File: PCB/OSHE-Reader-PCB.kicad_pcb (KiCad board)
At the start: 2 copper layers, 46 parts, among them Q1 Si1308EDL, Q2 BSS138, Q3 BSS138

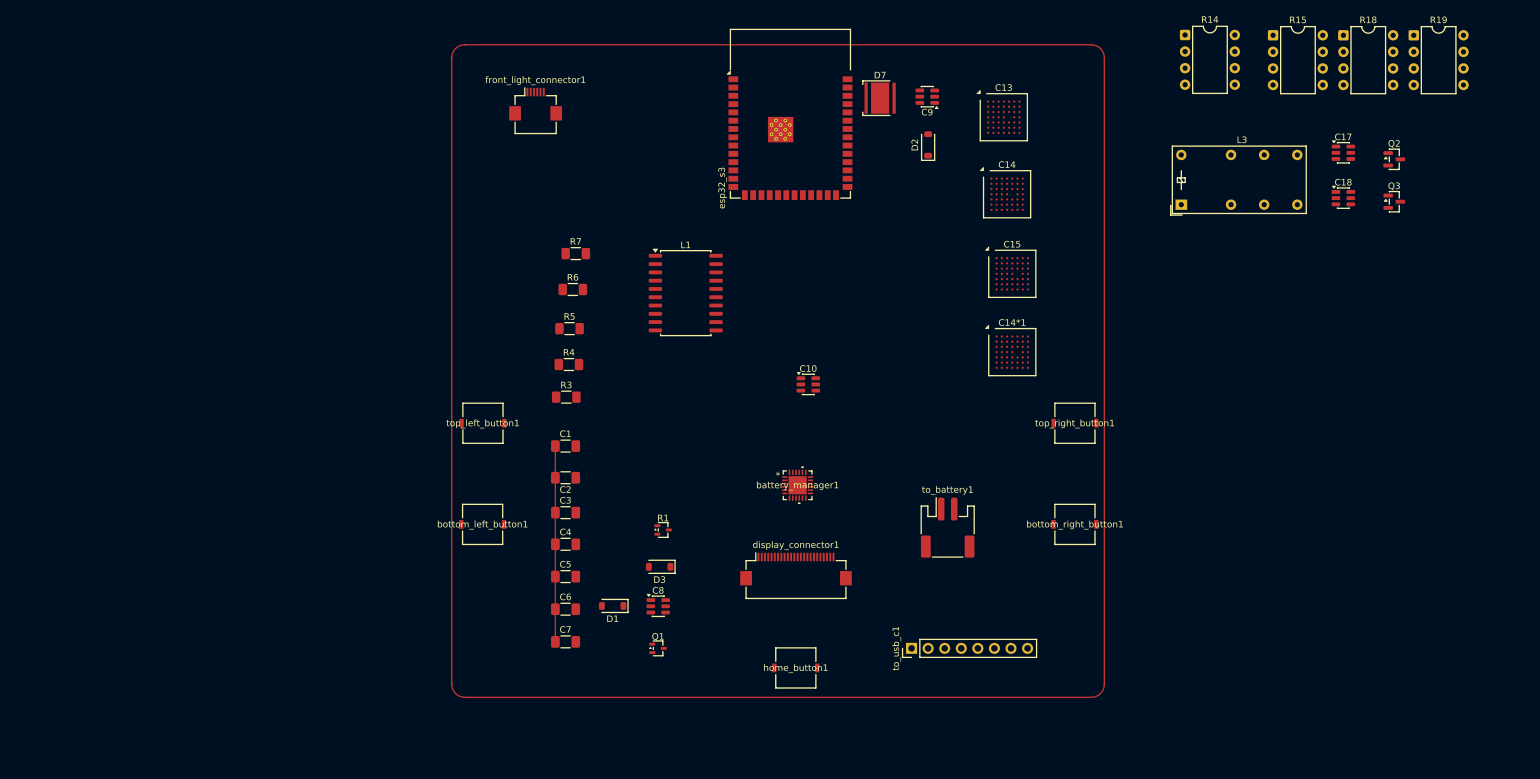
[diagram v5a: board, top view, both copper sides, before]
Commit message: PCB and BOM
Pulled stuff onto the PCB and regenerated the BOM to go into ours. Found some components (mostly caps and resistors) that are missing values so will need to update those.
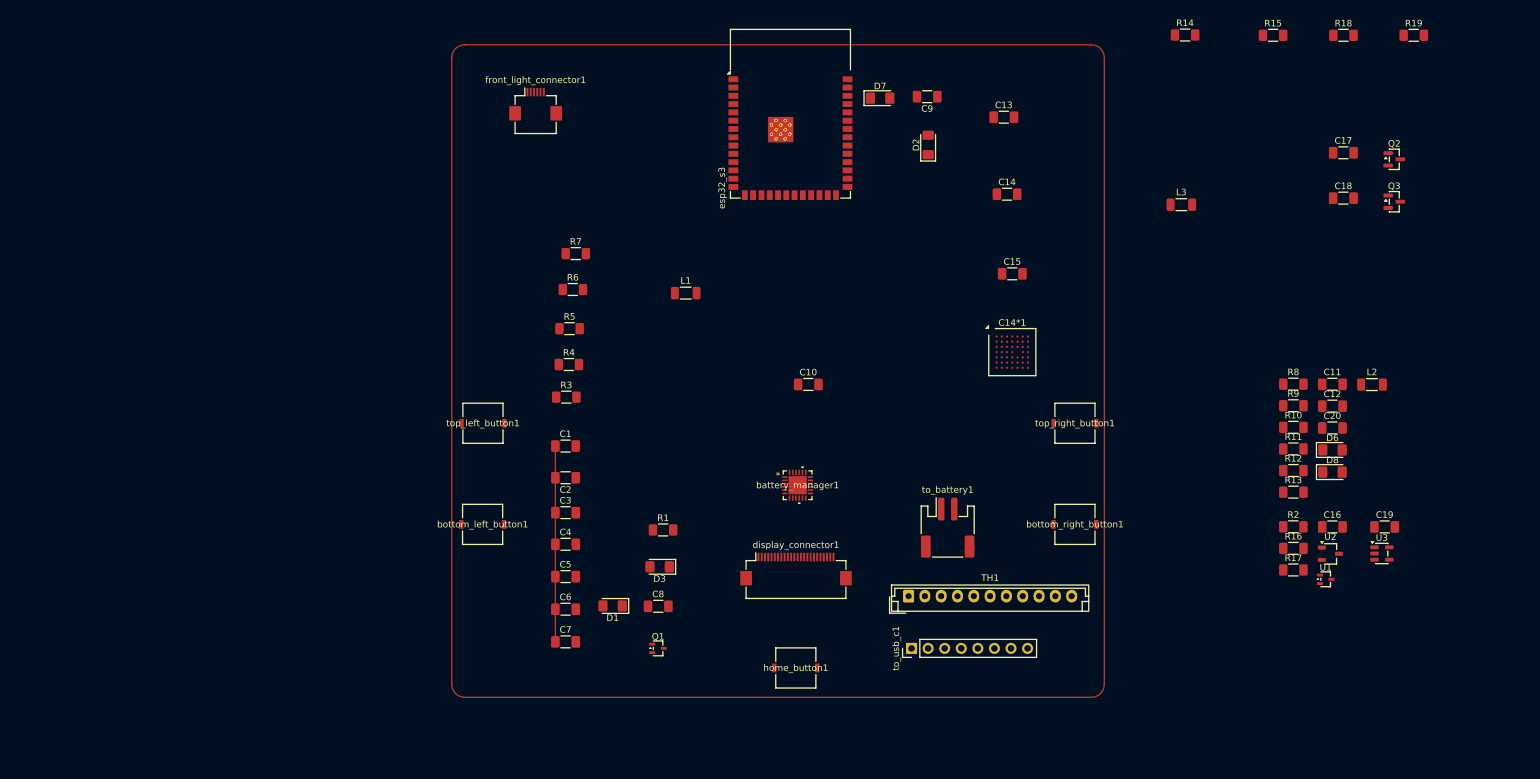
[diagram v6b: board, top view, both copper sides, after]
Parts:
- added C11: 1uF, Capacitor_SMD:C_1206_3216Metric_Pad1.33x1.80mm_HandSolder, F.Cu at (227.0, 90.0)
- added C12: 10uF, Capacitor_SMD:C_1206_3216Metric_Pad1.33x1.80mm_HandSolder, F.Cu at (227.0, 93.4)
- added C16: 0.1u, Capacitor_SMD:C_1206_3216Metric_Pad1.33x1.80mm_HandSolder, F.Cu at (227.0, 111.9)
- added C19: 10uF, Capacitor_SMD:C_1206_3216Metric_Pad1.33x1.80mm_HandSolder, F.Cu at (235.0, 111.9)
- added C20: 47nF, Capacitor_SMD:C_1206_3216Metric_Pad1.33x1.80mm_HandSolder, F.Cu at (227.0, 96.7)
- added D6: D_Schottky_Small_Filled, Diode_SMD:D_1206_3216Metric_Pad1.42x1.75mm_HandSolder, F.Cu at (227.0, 100.1)
- added D8: LED, LED_SMD:LED_1206_3216Metric_Pad1.42x1.75mm_HandSolder, F.Cu at (227.0, 103.5)
- added L2: 1uH, Inductor_SMD:L_1206_3216Metric_Pad1.22x1.90mm_HandSolder, F.Cu at (233.0, 90.1)
- added R10: R, Resistor_SMD:R_1206_3216Metric_Pad1.30x1.75mm_HandSolder, F.Cu at (221.0, 96.6)
- added R11: R, Resistor_SMD:R_1206_3216Metric_Pad1.30x1.75mm_HandSolder, F.Cu at (221.0, 99.9)
- added R12: R, Resistor_SMD:R_1206_3216Metric_Pad1.30x1.75mm_HandSolder, F.Cu at (221.0, 103.2)
- added R13: R, Resistor_SMD:R_1206_3216Metric_Pad1.30x1.75mm_HandSolder, F.Cu at (221.0, 106.6)
- added R16: 1M, Resistor_SMD:R_1206_3216Metric_Pad1.30x1.75mm_HandSolder, F.Cu at (221.0, 115.2)
- added R17: R_Small, Resistor_SMD:R_1206_3216Metric_Pad1.30x1.75mm_HandSolder, F.Cu at (221.0, 118.5)
- added R2: 1M, Resistor_SMD:R_1206_3216Metric_Pad1.30x1.75mm_HandSolder, F.Cu at (221.0, 111.9)
- added R8: R, Resistor_SMD:R_1206_3216Metric_Pad1.30x1.75mm_HandSolder, F.Cu at (221.0, 90.0)
- added R9: R, Resistor_SMD:R_1206_3216Metric_Pad1.30x1.75mm_HandSolder, F.Cu at (221.0, 93.3)
- added TH1: Thermistor, Connector_JST:JST_EH_B11B-EH-A_1x11_P2.50mm_Vertical, F.Cu at (162.0, 122.5)
- added U1: 74LVC1G04, Package_TO_SOT_SMD:SOT-323_SC-70, F.Cu at (225.9, 119.9)
- added U2: TPS923610DRLR, Package_TO_SOT_SMD:TSOT-23, F.Cu at (226.6, 116.0)
- added U3: TLV75533PDBV, Package_TO_SOT_SMD:SOT-23-5, F.Cu at (234.5, 116.0)
- C10, C17, C18, C8, C9: footprint Package_TO_SOT_SMD:SOT-23-6 -> Capacitor_SMD:C_1206_3216Metric_Pad1.33x1.80mm_HandSolder
- C13, C14, C15: footprint Package_CSP:Xilinx_CSG48_7.0x7.0mm_Layout7x7_P0.8mm -> Capacitor_SMD:C_1206_3216Metric_Pad1.33x1.80mm_HandSolder
- D1, D2, D3: footprint Diode_SMD:D_SOD-123 -> Diode_SMD:D_1206_3216Metric_Pad1.42x1.75mm_HandSolder
- D7: footprint LED_SMD:LED_Cree-XHP50_3V_HighDensity -> LED_SMD:LED_1206_3216Metric_Pad1.42x1.75mm_HandSolder
- L1: footprint Package_SO:SOIC-20W_7.5x12.8mm_P1.27mm -> Inductor_SMD:L_1206_3216Metric_Pad1.22x1.90mm_HandSolder
- L3: footprint Relay_THT:Relay_DPDT_Finder_30.22 -> Inductor_SMD:L_1206_3216Metric_Pad1.22x1.90mm_HandSolder
- R1: footprint Package_TO_SOT_SMD:SOT-323_SC-70 -> Resistor_SMD:R_1206_3216Metric_Pad1.30x1.75mm_HandSolder
- R14, R15, R18, R19: footprint Package_DIP:DIP-8_W7.62mm -> Resistor_SMD:R_1206_3216Metric_Pad1.30x1.75mm_HandSolder
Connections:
- D7 pad 2: /Battery Charger/PG -> /PG
- battery_manager1 pad 5: /Battery Charger/STAT -> /STAT
- battery_manager1 pad 6: /Battery Charger/GPIO_2 -> /OTG
- battery_manager1 pad 9: /Battery Charger/GPIO_1 -> /CE
- esp32_s3 pad 23: unconnected-(esp32_s3-IO21-Pad23) -> /PG
- esp32_s3 pad 31: unconnected-(esp32_s3-IO38-Pad31) -> /STAT
- esp32_s3 pad 38: unconnected-(esp32_s3-IO2-Pad38) -> /OTG
- esp32_s3 pad 39: unconnected-(esp32_s3-IO1-Pad39) -> /CE

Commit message: PCB Time
Started routing the PCB
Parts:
- moved C1 82.7 mm to (27.0, 93.5)
- moved C2 82.7 mm to (27.0, 98.3)
- moved C3 82.7 mm to (27.0, 103.7)
- moved C4 82.7 mm to (27.0, 108.5)
- moved C5 82.7 mm to (27.0, 113.5)
- moved C6 82.7 mm to (27.0, 118.5)
- moved C7 82.7 mm to (27.0, 123.5)
- moved D1 82.7 mm to (34.2, 118.0)
- moved R4 82.7 mm to (27.5, 81.0)
- moved R7 82.7 mm to (28.6, 64.0)
- moved L1 82.7 mm to (45.4, 70.1)
- moved Q1 82.7 mm to (41.2, 124.5)
- moved R3 82.7 mm to (27.1, 86.0)
- moved R5 82.7 mm to (27.6, 75.5)
- moved R6 82.7 mm to (28.1, 69.5)
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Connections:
- esp32_s3 pad 6: /BL_button -> /TL_button
- esp32_s3 pad 7: /TL_button -> /BL_button
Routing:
- net /BR_button: track 0.00 -> 88.8 mm, vias 0 -> 2
- net /BL_button: track 0.00 -> 78.1 mm
- net /TR_button: track 0.00 -> 74.7 mm, vias 0 -> 2
- net GND: track 30.0 -> 94.3 mm
- net /TL_button: track 0.00 -> 64.2 mm
- net /PG: track 0.00 -> 53.4 mm
- net /STAT: track 0.00 -> 50.8 mm
- net /BAT+: track 0.00 -> 44.4 mm
- net /Battery Charger/TS: track 0.00 -> 42.1 mm, vias 0 -> 1
- net /Battery Charger/REGN: track 0.00 -> 27.1 mm
- net unconnected-(display_connector1-MountPin-PadMP): track 0.00 -> 15.3 mm
- net /Display + Front Light/VGH: track 0.00 -> 15.0 mm
- net unconnected-(to_battery1-MountPin-PadMP): track 0.00 -> 6.70 mm
- net Net-(D1-K): track 0.00 -> 5.56 mm
- net Net-(D8-K): track 0.00 -> 5.55 mm
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
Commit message: More PCB work
ok so I had to restart the PCB
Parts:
- removed C14*1: 47nF, Package_CSP:Xilinx_CSG48_7.0x7.0mm_Layout7x7_P0.8mm
- moved R19 235.0 mm to (27.5, 138.1)
- moved R18 223.9 mm to (27.5, 134.8)
- moved R15 209.9 mm to (27.5, 124.9)
- moved C17 197.1 mm to (45.5, 127.3)
- moved C18 195.8 mm to (45.5, 130.6)
- moved Q2 193.9 mm to (52.1, 115.5)
- moved U3 193.5 mm to (37.3, 105.0)
- moved Q3 193.3 mm to (52.1, 120.0)
- moved R14 190.5 mm to (27.5, 121.6), turned to 0 degrees
- moved L3 188.9 mm to (33.5, 144.2)
- moved C9 187.9 mm to (39.5, 134.0), turned to 0 degrees
- moved R2 187.9 mm to (27.5, 118.3)
- moved R16 187.6 mm to (27.5, 128.2)
- moved R17 187.6 mm to (27.5, 131.5)
- moved U1 181.4 mm to (38.5, 144.1)
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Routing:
- net /PG: track 53.4 -> 2.50 mm, vias 0 -> 1
- net /Battery Charger/TS: track 42.1 -> 0.00 mm, vias 1 -> 0
- net /BAT+: track 44.4 -> 13.1 mm
- net /STAT: track 50.8 -> 79.9 mm, vias 0 -> 2
- net /Battery Charger/REGN: track 27.1 -> 0.00 mm
- net GND: track 94.3 -> 72.4 mm
- net /3V3: track 0.00 -> 18.0 mm
- net /BR_button: track 88.8 -> 105.8 mm
- net /Display + Front Light/VGH: track 15.0 -> 0.00 mm
- net /TR_button: track 74.7 -> 88.3 mm
- net /TL_button: track 64.2 -> 73.2 mm
- net /Battery Charger/SW: track 0.00 -> 7.93 mm
- net /VBUS: track 0.00 -> 7.62 mm
- net /BL_button: track 78.1 -> 84.7 mm
- net /Battery Charger/SYS: track 0.00 -> 6.55 mm
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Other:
- board outline added: 100 x 100 mm
